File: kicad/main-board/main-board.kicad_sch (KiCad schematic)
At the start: 2 parts, among them J1 Conn_01x02, U1 CM5108064B

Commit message: made overall schematic
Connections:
- net +5V(INPUT): now also J1.1 (Pin_1)
- net GND: now also J1.2 (Pin_2)
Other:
- sheet Ports: file Ports.kicad_sch -> ../main-board/Ports.kicad_sch
- sheet Ports ports: added GND; removed none
- moved on the sheet: J1

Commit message: worked on main board
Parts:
- added C53: 10u, Capacitor_SMD:C_0805_2012Metric, symbol Device:C
- added J8: Micro_SD_Card_Det, CM5IO:SDCARD_MOLEX_503398-1892, symbol Connector:Micro_SD_Card_Det2
- added R47: 10K 1%, Resistor_SMD:R_0402_1005Metric, symbol Device:R
- added U18: RT9742GGJ5, Package_TO_SOT_SMD:SOT-23-5, symbol CM5IO:RT9742GGJ5
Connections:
- net GND: now also C53.2, J8.11 (SHIELD), J8.6 (VSS), U18.2 (GND)
- net SD_CLK: now reaches U1.57 (SD_CLK)
- net SD_CLK: now also J8.5 (CLK)
- net SD_DAT3: now reaches U1.61 (SD_DAT3)
- net SD_DAT3: now also J8.2 (DAT3/CD)
- net SD_CMD: now reaches U1.62 (SD_CMD)
- net SD_CMD: now also J8.3 (CMD)
- net SD_DAT0: now reaches U1.63 (SD_DAT0)
- net SD_DAT0: now also J8.7 (DAT0)
- net SD_DAT1: now reaches U1.67 (SD_DAT1)
- net SD_DAT1: now also J8.8 (DAT1)
- net SD_DAT2: now reaches U1.69 (SD_DAT2)
- net SD_DAT2: now also J8.1 (DAT2)
- net SD_PWR_ON: now reaches U1.75 (SD_PWR_ON)
- net SD_PWR_ON: now also R47.2, U18.4 (EN)
- new net +3.3v: R47.1, U18.5 (IN)
- new net SD_PWR: C53.1, J8.4 (VDD), U18.1 (OUT)
- no-connect marks 0 -> 8
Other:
- note added: "CM5Lite SDCARD I/F"
- moved on the sheet: J1, U1A

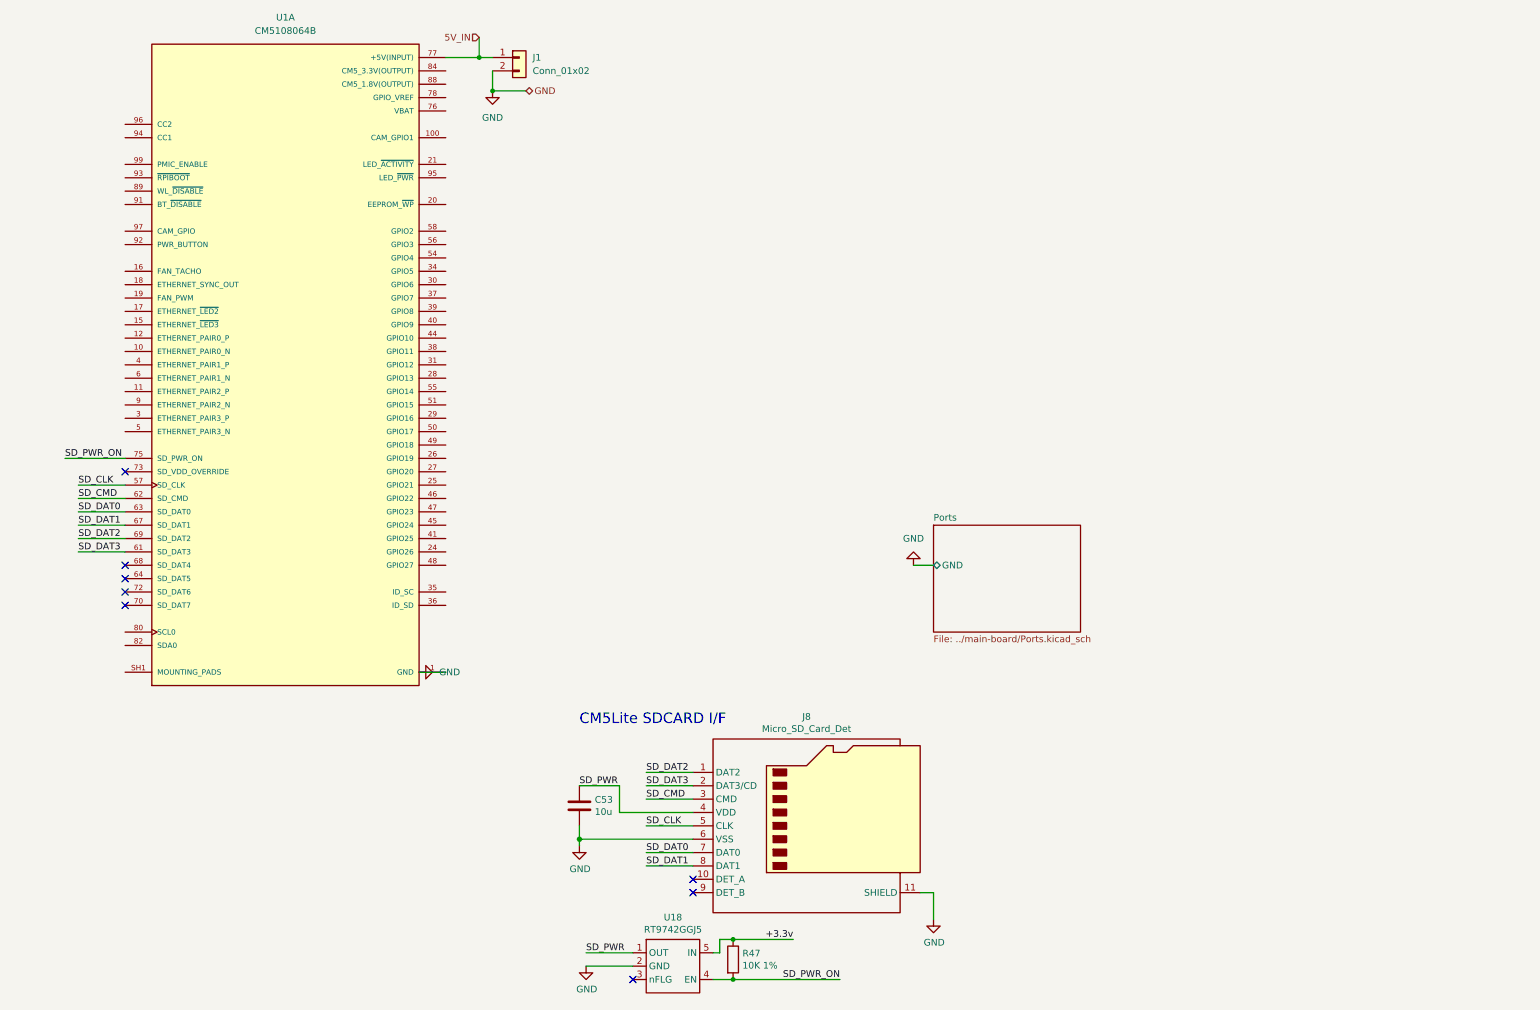
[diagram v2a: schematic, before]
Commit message: updated the main board, changes journaled in the fallout journaling
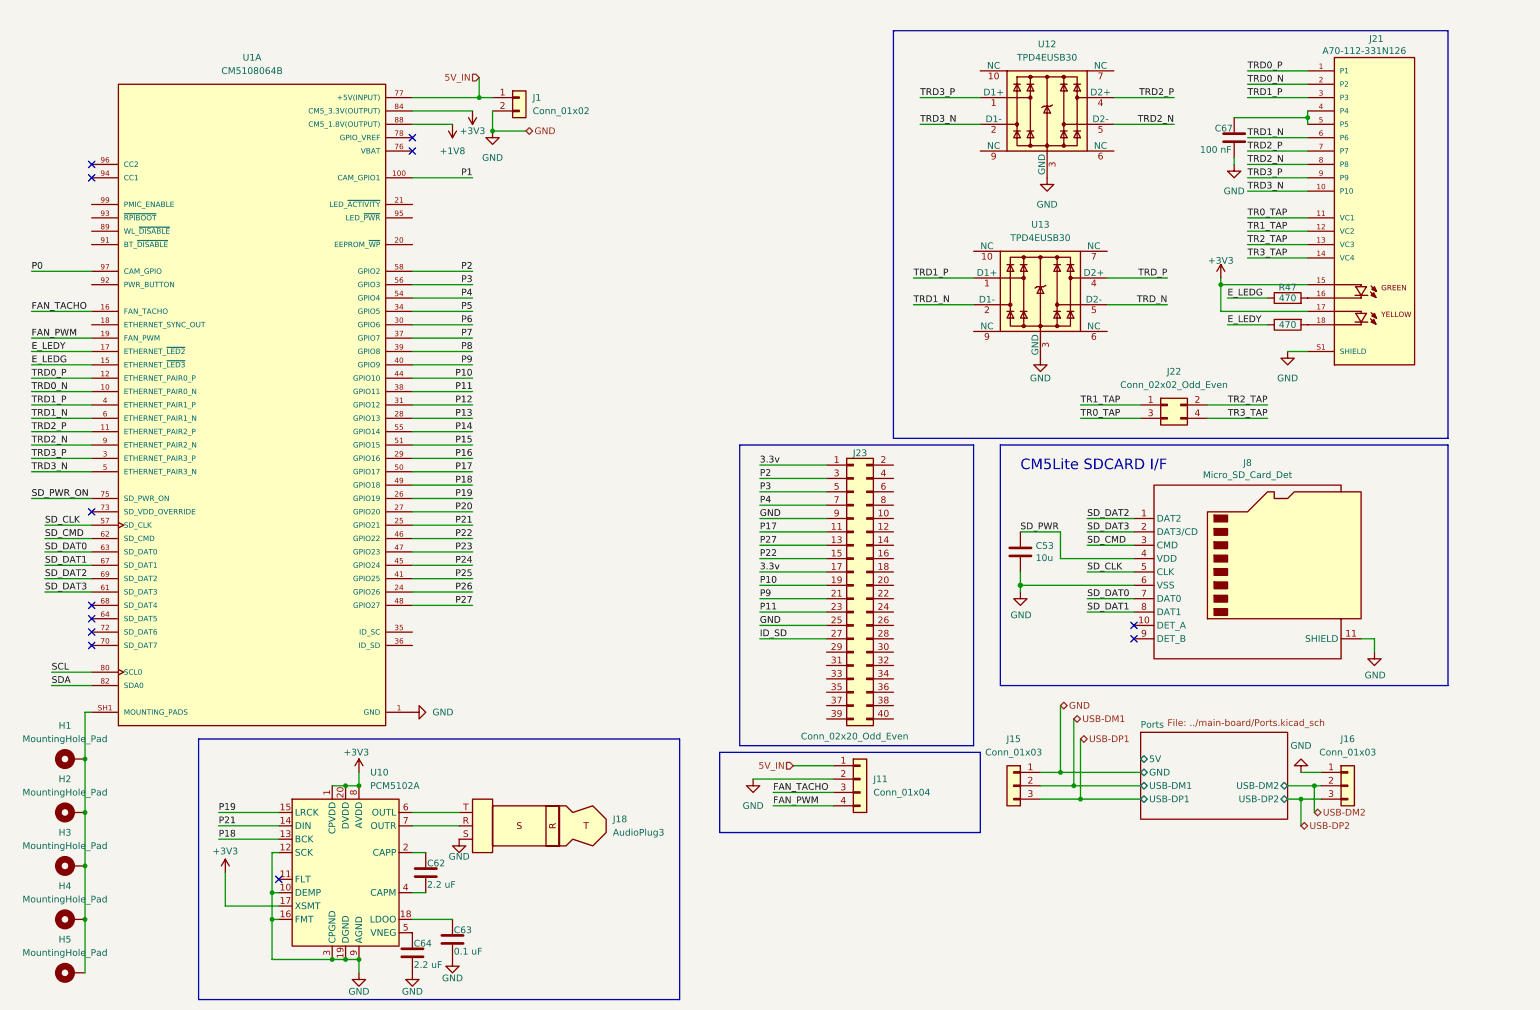
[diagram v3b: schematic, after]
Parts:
- removed U18: RT9742GGJ5, Package_TO_SOT_SMD:SOT-23-5, symbol CM5IO:RT9742GGJ5
- added C62, C64: 2.2 uF, symbol Device:C
- added C63: 0.1 uF, symbol Device:C
- added C67: 100 nF, symbol Device:C
- added H1, H2, H3, H4, H5: MountingHole_Pad, symbol Mechanical:MountingHole_Pad
- added J11: Conn_01x04, symbol Connector_Generic:Conn_01x04
- added J15, J16: Conn_01x03, symbol Connector_Generic:Conn_01x03
- added J18: AudioPlug3, symbol Connector_Audio:AudioPlug3
- added J21: A70-112-331N126, A70-112-331N126:EDAC_A70-112-331N126, symbol A70-112-331N126:A70-112-331N126
- added J22: Conn_02x02_Odd_Even, symbol Connector_Generic:Conn_02x02_Odd_Even
- added J23: Conn_02x20_Odd_Even, symbol Connector_Generic:Conn_02x20_Odd_Even
- added R50: 470, symbol Device:R
- added U10: PCM5102A, Package_SO:TSSOP-20_4.4x6.5mm_P0.65mm, symbol Audio:PCM5102A
- added U12, U13: TPD4EUSB30, Package_SON:USON-10_2.5x1.0mm_P0.5mm, symbol Power_Protection:TPD4EUSB30
- R47: value 10K 1% -> 470; footprint Resistor_SMD:R_0402_1005Metric -> (none); Field4 Farnell -> (none); Field6 MCR01MZPF1002 -> (none); Field7 Rohm -> (none); Part Description Resistor 10K M1005 1% 63mW -> (none)
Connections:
- net +3.3v is gone; now on net E_LEDG: R47.1
- net +5V(INPUT): now also J11.1 (Pin_1)
- net GND: now also C63.2, C64.2, C67.2, J11.2 (Pin_2), J15.1 (Pin_1), J16.1 (Pin_1), J18.S, J21.S1 (SHIELD), J21.S2 (SHIELD), J23.25 (Pin_25), J23.9 (Pin_9), U10.10 (DEMP), U10.12 (SCK), U10.16 (FMT), U10.19 (DGND), U10.3 (CPGND), U10.9 (AGND), U12.3 (GND), U12.8 (GND), U13.3 (GND), U13.8 (GND)
- net SD_PWR_ON: no longer R47.2
- net TRD0_N: now reaches U1.10 (ETHERNET_PAIR0_N)
- net TRD0_N: now also J21.2 (P2)
- net P1: now reaches U1.100 (CAM_GPIO1)
- net TRD2_P: now reaches U1.11 (ETHERNET_PAIR2_P)
- net TRD2_P: now also J21.7 (P7), U12.4 (D2+)
- net TRD0_P: now reaches U1.12 (ETHERNET_PAIR0_P)
- net TRD0_P: now also J21.1 (P1)
- net E_LEDG: now reaches U1.15 (ETHERNET_~{LED3})
- net FAN_TACHO: now reaches U1.16 (FAN_TACHO)
- net FAN_TACHO: now also J11.3 (Pin_3)
- net E_LEDY: now reaches U1.17 (ETHERNET_~{LED2})
- net E_LEDY: now also R50.1
- net FAN_PWM: now reaches U1.19 (FAN_PWM)
- net FAN_PWM: now also J11.4 (Pin_4)
- net P26: now reaches U1.24 (GPIO26)
- net P21: now reaches U1.25 (GPIO21)
- net P21: now also U10.14 (DIN)
- net P19: now reaches U1.26 (GPIO19)
- net P19: now also U10.15 (LRCK)
- net P20: now reaches U1.27 (GPIO20)
- net P13: now reaches U1.28 (GPIO13)
- net P16: now reaches U1.29 (GPIO16)
- net TRD3_P: now reaches U1.3 (ETHERNET_PAIR3_P)
- net TRD3_P: now also J21.9 (P9), U12.1 (D1+)
- net P6: now reaches U1.30 (GPIO6)
- net P12: now reaches U1.31 (GPIO12)
- net P5: now reaches U1.34 (GPIO5)
- net P7: now reaches U1.37 (GPIO7)
- net P11: now reaches U1.38 (GPIO11)
- net P11: now also J23.23 (Pin_23)
- net P8: now reaches U1.39 (GPIO8)
- net TRD1_P: now reaches U1.4 (ETHERNET_PAIR1_P)
- net TRD1_P: now also J21.3 (P3), U13.1 (D1+)
- net P9: now reaches U1.40 (GPIO9)
- net P9: now also J23.21 (Pin_21)
- net P25: now reaches U1.41 (GPIO25)
- net P10: now reaches U1.44 (GPIO10)
- net P10: now also J23.19 (Pin_19)
- net P24: now reaches U1.45 (GPIO24)
- net P22: now reaches U1.46 (GPIO22)
- net P22: now also J23.15 (Pin_15)
- net P23: now reaches U1.47 (GPIO23)
- net P27: now reaches U1.48 (GPIO27)
- net P27: now also J23.13 (Pin_13)
- net P18: now reaches U1.49 (GPIO18)
- net P18: now also U10.13 (BCK)
- net TRD3_N: now reaches U1.5 (ETHERNET_PAIR3_N)
- net TRD3_N: now also J21.10 (P10), U12.2 (D1-)
- net P17: now reaches U1.50 (GPIO17)
- net P17: now also J23.11 (Pin_11)
- net P15: now reaches U1.51 (GPIO15)
- net P4: now reaches U1.54 (GPIO4)
- net P4: now also J23.7 (Pin_7)
- net P14: now reaches U1.55 (GPIO14)
- net P3: now reaches U1.56 (GPIO3)
- net P3: now also J23.5 (Pin_5)
- net P2: now reaches U1.58 (GPIO2)
- net P2: now also J23.3 (Pin_3)
- net TRD1_N: now reaches U1.6 (ETHERNET_PAIR1_N)
- net TRD1_N: now also J21.6 (P6), U13.2 (D1-)
- net SCL: now reaches U1.80 (SCL0)
- net SDA: now reaches U1.82 (SDA0)
- net TRD2_N: now reaches U1.9 (ETHERNET_PAIR2_N)
- net TRD2_N: now also J21.8 (P8), U12.5 (D2-)
- net P0: now reaches U1.97 (CAM_GPIO)
- net at U1.SH1 (MOUNTING_PADS), U1.SH2 (MOUNTING_PADS), U1.SH3 (MOUNTING_PADS)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: now also H1.1, H2.1, H3.1, H4.1, H5.1
- net CM5_1.8V(OUTPUT) renamed +1V8
- net CM5_3.3V(OUTPUT) renamed +3V3
- net +3V3: now also J21.15, J21.17, U10.1 (CPVDD), U10.17 (XSMT), U10.20 (DVDD), U10.8 (AVDD)
- new net: C63.1, U10.18 (LDOO)
- new net: C67.1, J21.4 (P4), J21.5 (P5)
- new net: J21.16, R47.2
- new net: J18.R, U10.7 (OUTR)
- new net: J18.T, U10.6 (OUTL)
- new net: C64.1, U10.5 (VNEG)
- new net: J21.18, R50.2
- new net: C62.1, U10.2 (CAPP)
- new net: C62.2, U10.4 (CAPM)
- new net 3.3v: J23.1 (Pin_1), J23.17 (Pin_17)
- new net ID_SD: J23.27 (Pin_27)
- new net TR0_TAP: J21.11 (VC1), J22.3 (Pin_3)
- new net TR1_TAP: J21.12 (VC2), J22.1 (Pin_1)
- new net TR2_TAP: J21.13 (VC3), J22.2 (Pin_2)
- new net TR3_TAP: J21.14 (VC4), J22.4 (Pin_4)
- new net TRD_N: U13.5 (D2-)
- new net TRD_P: U13.4 (D2+)
- new net USB-DM1: J15.2 (Pin_2)
- new net USB-DM2: J16.2 (Pin_2)
- new net USB-DP1: J15.3 (Pin_3)
- new net USB-DP2: J16.3 (Pin_3)
- no-connect marks 8 -> 12
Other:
- sheet Ports ports: added 5V, USB-DM1, USB-DM2, USB-DP1, USB-DP2; removed none
- moved on the sheet: C53, J1, J8, U1A

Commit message: Completed the main board schematic
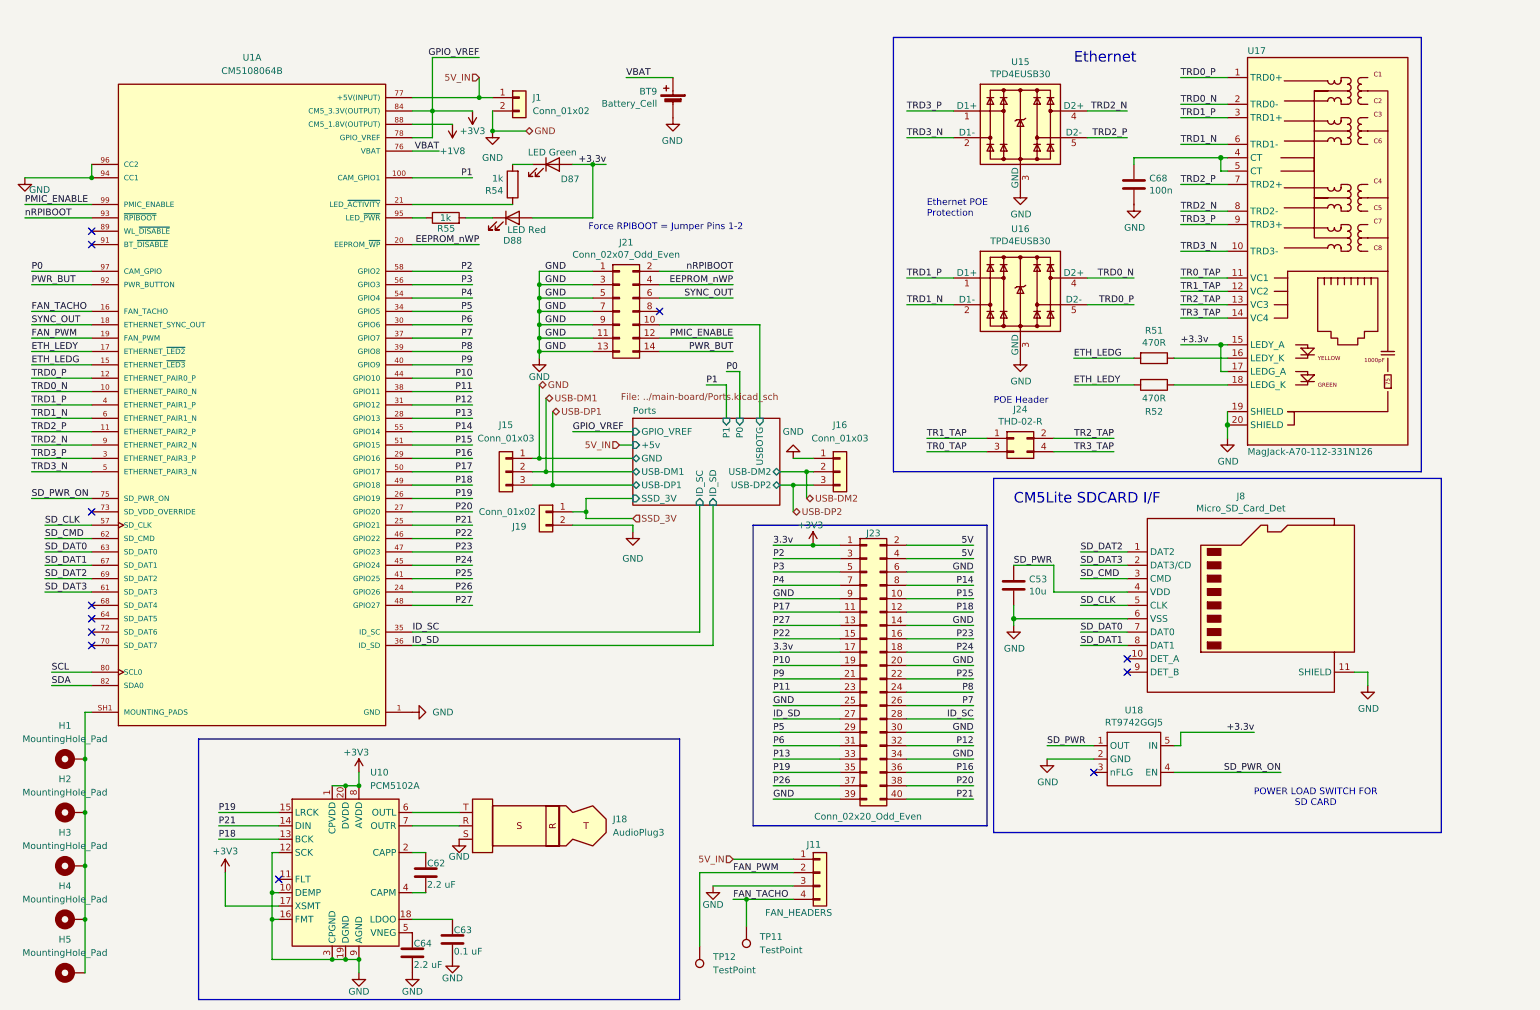
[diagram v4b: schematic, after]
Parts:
- removed C67: 100 nF, symbol Device:C
- removed J21: A70-112-331N126, A70-112-331N126:EDAC_A70-112-331N126, symbol A70-112-331N126:A70-112-331N126
- removed J22: Conn_02x02_Odd_Even, symbol Connector_Generic:Conn_02x02_Odd_Even
- removed R47, R50: 470, symbol Device:R
- removed U12, U13: TPD4EUSB30, Package_SON:USON-10_2.5x1.0mm_P0.5mm, symbol Power_Protection:TPD4EUSB30
- added BT9: Battery_Cell, CM5IO:BatteryHolder_Keystone_3034_1x20mm, symbol Device:Battery_Cell
- added C68: 100n, Capacitor_SMD:C_0402_1005Metric, symbol Device:C
- added D87: LED Green, LED_SMD:LED_0603_1608Metric, symbol Device:LED
- added D88: LED Red, LED_SMD:LED_0603_1608Metric, symbol Device:LED
- added J19: Conn_01x02, symbol Connector_Generic:Conn_01x02
- added J21: Conn_02x07_Odd_Even, Connector_PinHeader_2.54mm:PinHeader_2x07_P2.54mm_Vertical, symbol Connector_Generic:Conn_02x07_Odd_Even
- added J24: THD-02-R, Connector_PinHeader_2.54mm:PinHeader_2x02_P2.54mm_Vertical, symbol Connector_Generic:Conn_02x02_Odd_Even
- added R51, R52: 470R, Resistor_SMD:R_0402_1005Metric, symbol Device:R
- added R54, R55: 1k, Resistor_SMD:R_0402_1005Metric, symbol Device:R
- added TP11, TP12: TestPoint, symbol Connector:TestPoint
- added U15, U16: TPD4EUSB30, Package_SON:USON-10_2.5x1.0mm_P0.5mm, symbol CM5IO:TPD4EUSB30
- added U17: MagJack-A70-112-331N126, CM5IO:TRJG0926HENL, symbol CM5IO:MagJack-A70-112-331N126
- added U18: RT9742GGJ5, Package_TO_SOT_SMD:SOT-23-5, symbol CM5IO:RT9742GGJ5
- J11: value Conn_01x04 -> FAN_HEADERS
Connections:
- net 3.3v is gone; now on net +3V3: J23.1 (Pin_1), J23.17 (Pin_17)
- net +3V3: now also U1.78 (GPIO_VREF)
- net FAN_PWM: now also J11.2 (Pin_2), TP12.1; no longer J11.4 (Pin_4)
- net FAN_TACHO: now also J11.4 (Pin_4), TP11.1; no longer J11.3 (Pin_3)
- net GND: now also J11.3 (Pin_3), J23.14 (Pin_14), J23.20 (Pin_20), J23.30 (Pin_30), J23.34 (Pin_34), J23.39 (Pin_39), J23.6 (Pin_6), U1.94 (CC1), U1.96 (CC2), BT9.2 (-), C68.2, J19.2 (Pin_2), J21.1 (Pin_1), J21.11 (Pin_11), J21.13 (Pin_13), J21.3 (Pin_3), J21.5 (Pin_5), J21.7 (Pin_7), J21.9 (Pin_9), U15.3 (GND), U15.8 (GND), U16.3 (GND), U16.8 (GND), U17.19 (SHIELD), U17.20 (SHIELD), U18.2 (GND); no longer J11.2 (Pin_2)
- net ID_SD: now also U1.36 (ID_SD)
- net P12: now also J23.32 (Pin_32)
- net P13: now also J23.33 (Pin_33)
- net P14: now also J23.8 (Pin_8)
- net P15: now also J23.10 (Pin_10)
- net P16: now also J23.36 (Pin_36)
- net P18: now also J23.12 (Pin_12)
- net P19: now also J23.35 (Pin_35)
- net P20: now also J23.38 (Pin_38)
- net P21: now also J23.40 (Pin_40)
- net P23: now also J23.16 (Pin_16)
- net P24: now also J23.18 (Pin_18)
- net P25: now also J23.22 (Pin_22)
- net P26: now also J23.37 (Pin_37)
- net P5: now also J23.29 (Pin_29)
- net P6: now also J23.31 (Pin_31)
- net P7: now also J23.26 (Pin_26)
- net P8: now also J23.24 (Pin_24)
- net SD_PWR: now also U18.1 (OUT)
- net SD_PWR_ON: now also U18.4 (EN)
- net TR0_TAP: now also J24.3 (Pin_3), U17.11 (VC1)
- net TR1_TAP: now also J24.1 (Pin_1), U17.12 (VC2)
- net TR2_TAP: now also J24.2 (Pin_2), U17.13 (VC3)
- net TR3_TAP: now also J24.4 (Pin_4), U17.14 (VC4)
- net TRD0_N: now also U16.4 (D2+), U16.7, U17.2 (TRD0-)
- net TRD0_P: now also U16.5 (D2-), U16.6, U17.1 (TRD0+)
- net TRD1_N: now also U16.2 (D1-), U16.9, U17.6 (TRD1-)
- net TRD1_P: now also U16.1 (D1+), U16.10, U17.3 (TRD1+)
- net TRD2_N: now also U15.4 (D2+), U15.7, U17.8 (TRD2-)
- net TRD2_P: now also U15.5 (D2-), U15.6, U17.7 (TRD2+)
- net TRD3_N: now also U15.2 (D1-), U15.9, U17.10 (TRD3-)
- net TRD3_P: now also U15.1 (D1+), U15.10, U17.9 (TRD3+)
- net SYNC_OUT: now reaches U1.18 (ETHERNET_SYNC_OUT)
- net SYNC_OUT: now also J21.6 (Pin_6)
- net EEPROM_nWP: now reaches U1.20 (EEPROM_~{WP})
- net EEPROM_nWP: now also J21.4 (Pin_4)
- net at U1.21 (LED_~{ACTIVITY}): now also R54.1
- net at U1.35 (ID_SC): no longer names the net of U1.35 (ID_SC)
- net at U1.35 (ID_SC): now also J23.28 (Pin_28)
- net VBAT: now reaches U1.76 (VBAT)
- net VBAT: now also BT9.1 (+)
- net PWR_BUT: now reaches U1.92 (PWR_BUTTON)
- net PWR_BUT: now also J21.14 (Pin_14)
- net nRPIBOOT: now reaches U1.93 (~{RPIBOOT})
- net nRPIBOOT: now also J21.2 (Pin_2)
- net at U1.95 (LED_~{PWR}): now also R55.1
- net PMIC_ENABLE: now reaches U1.99 (PMIC_ENABLE)
- net PMIC_ENABLE: now also J21.12 (Pin_12)
- net 5V: now reaches J23.2 (Pin_2)
- net 5V: now also J23.4 (Pin_4)
- net E_LEDG renamed ETH_LEDG
- net ETH_LEDG: now also R51.2
- net E_LEDY renamed ETH_LEDY
- net ETH_LEDY: now also R52.2
- new net: D87.1 (K), R54.2
- new net: R51.1, U17.16 (LEDY_K)
- new net: R52.1, U17.18 (LEDG_K)
- new net: C68.1, U17.4 (CT), U17.5 (CT)
- new net: D88.1 (K), R55.2
- new net +3.3v: D87.2 (A), D88.2 (A), U17.15 (LEDY_A), U17.17 (LEDG_A), U18.5 (IN)
- new net Ports/USBOTG: J21.10 (Pin_10)
- new net SSD_3V: J19.1 (Pin_1)
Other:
- sheet Ports ports: added +5v, GPIO_VREF, ID_SC, ID_SD, P0, P1, SSD_3V, USBOTG; removed 5V
- note added: "Ethernet"
- note added: "Ethernet POE Protection"
- note added: "Force RPIBOOT = Jumper Pins 1-2"
- note added: "POE Header"
- note added: "POWER LOAD SWITCH FOR SD CARD"
- moved on the sheet: C53, J11, J15, J16, J23, J8

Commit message: finally completed the schematic
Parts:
- added J10: Conn_01x08, symbol Connector_Generic:Conn_01x08
- added J3, J8: Conn_01x03, symbol Connector_Generic:Conn_01x03
- renumbered BT9 to BT1, C68 to C1, C53 to C2, C62 to C3, C63 to C4, C64 to C5, D87 to D1, D88 to D2, J23 to J11, J18 to J12, J11 to J13, J21 to J2, J16 to J4, J24 to J5, J15 to J6, J19 to J7, J8 to J9, R54 to R1, R55 to R2, R51 to R3, R52 to R4, TP11 to TP1, TP12 to TP2, U15 to U1, U16 to U2, U1 to U3, U17 to U4, U18 to U5, U10 to U6
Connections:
- net +3V3: no longer J11.1 (Pin_1), J11.17 (Pin_17), U3.78 (GPIO_VREF), U3.84 (CM5_3.3V(OUTPUT)), U3.86 (CM5_3.3V(OUTPUT))
- net GND: now also J3.1 (Pin_1), J8.1 (Pin_1)
- net P10 renamed MOSI
- net MOSI: now also J10.6 (Pin_6)
- net P11 renamed SCK
- net SCK: now also J10.8 (Pin_8)
- net P17 renamed GPI017
- net GPI017: now also J10.4 (Pin_4)
- net P22 renamed GPIO22
- net GPIO22: now also J10.3 (Pin_3)
- net P27 renamed GPIO27
- net GPIO27: now also J10.5 (Pin_5)
- net P5 renamed GPIO5
- net GPIO5: now also J10.2 (Pin_2)
- net P8 renamed CE0
- net CE0: now also J10.1 (Pin_1)
- net P9 renamed MISO
- net MISO: now also J10.7 (Pin_7)
- new net CM5_3.3V(OUTPUT): J11.1 (Pin_1), J11.17 (Pin_17), U3.78 (GPIO_VREF), U3.84 (CM5_3.3V(OUTPUT)), U3.86 (CM5_3.3V(OUTPUT))
- new net Ports/USB-DM4: J3.2 (Pin_2)
- new net USB-DM3: J8.2 (Pin_2)
- new net USB-DP3: J8.3 (Pin_3)
- new net USB-DP4: J3.3 (Pin_3)
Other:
- sheet Ports ports: added SCL, SDA, USB-DM3, USB-DM4, USB-DP3, USB-DP4; removed none
- note added: "CIPHER - by ARYAN-GIT-BYTE"
- moved on the sheet: J11, J2, J4
